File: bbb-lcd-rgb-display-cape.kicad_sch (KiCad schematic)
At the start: 28 parts, among them P12 RS485, P8 BeagleBone_Black_Header, P9 BeagleBone_Black_Header, Sw1 DTSM-31N, Sw2 DTSM-31N, Sw3 DTSM-31N, Sw4 DTSM-31N, U5 TCN75A, U6 DS18B20U

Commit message: Continue schematic work
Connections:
- net BACKLIGHT_PWM: now reaches P8.13 (Pin_13)
- net R1: now reaches P8.15 (Pin_15)
- net R0: now reaches P8.16 (Pin_16)
- net VSYNC: now reaches P8.27 (Pin_27)
- net PCLK: now reaches P8.28 (Pin_28)
- net HSYNC: now reaches P8.29 (Pin_29)
- net DE: now reaches P8.30 (Pin_30)
- net R3: now reaches P8.31 (Pin_31)
- net R2: now reaches P8.32 (Pin_32)
- net R4: now reaches P8.33 (Pin_33)
- net G0: now reaches P8.34 (Pin_34)
- net R5: now reaches P8.35 (Pin_35)
- net G1: now reaches P8.36 (Pin_36)
- net G3: now reaches P8.37 (Pin_37)
- net G2: now reaches P8.38 (Pin_38)
- net G5: now reaches P8.39 (Pin_39)
- net G4: now reaches P8.40 (Pin_40)
- net B1: now reaches P8.41 (Pin_41)
- net B0: now reaches P8.42 (Pin_42)
- net B3: now reaches P8.43 (Pin_43)
- net B2: now reaches P8.44 (Pin_44)
- net B5: now reaches P8.45 (Pin_45)
- net B4: now reaches P8.46 (Pin_46)
- no-connect marks 52 -> 29
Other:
- sheet LCD Display ports: added BACKLIGHT_PWM, LCD_CS, LCD_D0(B1), LCD_D1(B2), LCD_D10(G5), LCD_D11(R1), LCD_D12(R2), LCD_D13(R3), LCD_D14(R4), LCD_D15(R5), LCD_D2(B3), LCD_D3(B4), LCD_D4(B5), LCD_D5(G0), LCD_D6(G1), LCD_D7(G2), LCD_D8(G3), LCD_D9(G4), LCD_FMARK(PCLK), LCD_RD(VSYNC), LCD_RS(HSYNC), LCD_RST, LCD_SPI_CLK, LCD_SPI_CS0, LCD_SPI_DIO, LCD_WR(DE), POWER_SUPPLY_2.7-5.5V, POWER_SUPPLY_2.7-5.5V_GND, TP_I2C_SCL, TP_I2C_SDA, TP_IRQ, TP_SHUTDOWN; removed none
- moved on the sheet: P8

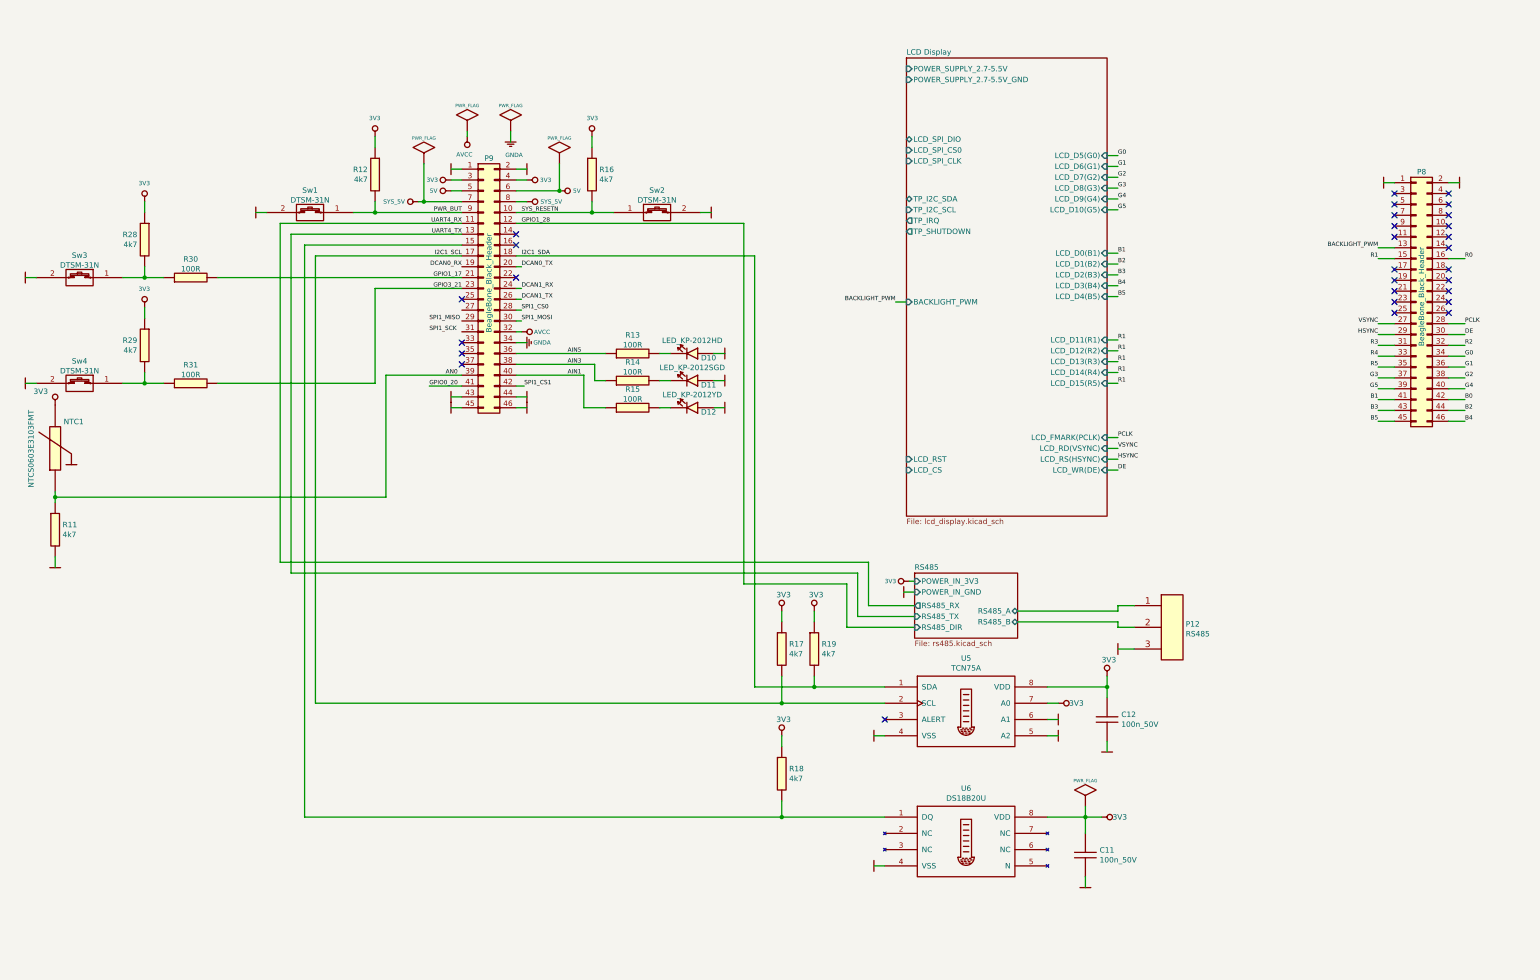
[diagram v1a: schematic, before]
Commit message: Corrected schematic and added new elements
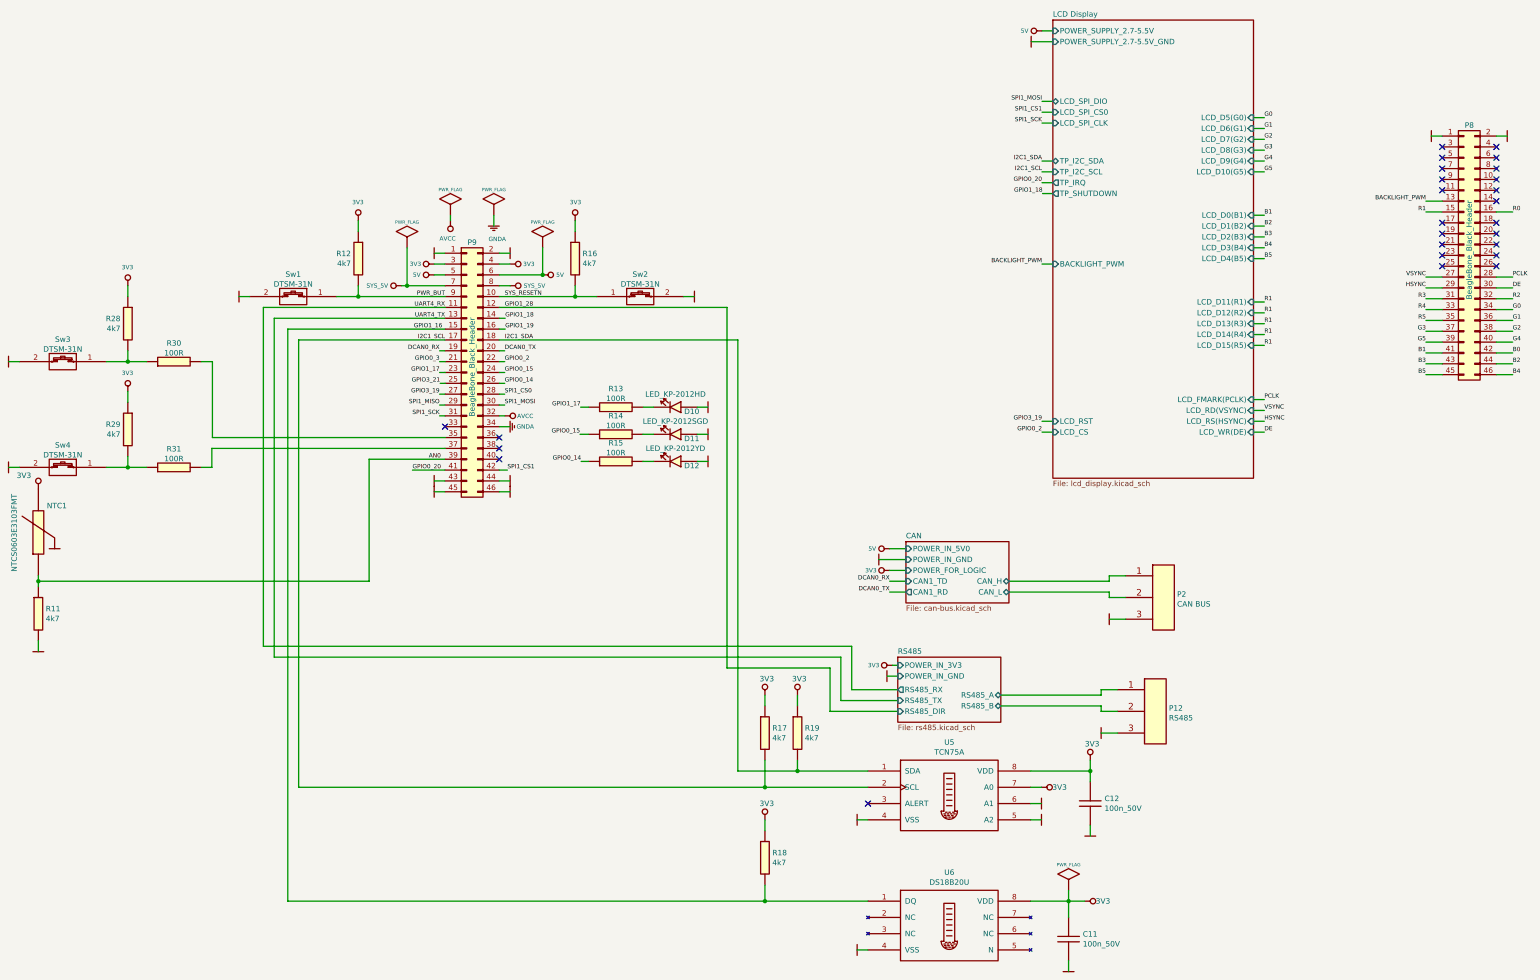
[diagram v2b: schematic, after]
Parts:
- added P2: CAN BUS, Discrete_Connectors:DG301-5.0-03P-12-00A(H), symbol Discrete_Connectors:DG301-5.0-03P-12-00A(H)
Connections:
- net GND: now also P2.3
- net GPIO1_17: now also P9.23 (Pin_23), R13.1; no longer P9.21 (Pin_21), R30.2
- net GPIO3_21: now also P9.25 (Pin_25); no longer P9.23 (Pin_23), R31.2
- net SPI1_MISO: now also P9.29 (Pin_29)
- net SPI1_SCK: now also P9.31 (Pin_31)
- net GPIO1_18: now reaches P9.14 (Pin_14)
- net GPIO1_16: now reaches P9.15 (Pin_15), R18.2, U6.1 (DQ)
- net GPIO1_19: now reaches P9.16 (Pin_16)
- net GPIO0_2: now reaches P9.22 (Pin_22)
- net GPIO3_19: now reaches P9.27 (Pin_27)
- net at P9.35 (Pin_35): now also R30.2
- net at P9.37 (Pin_37): now also R31.2
- net AIN1: no longer names the net of P9.40 (Pin_40)
- net AIN1: no longer R15.1
- net AIN3: no longer names the net of P9.38 (Pin_38)
- net AIN3: no longer R14.1
- net AIN5: no longer names the net of P9.36 (Pin_36)
- net AIN5: no longer R13.1
- net DCAN1_RX renamed GPIO0_15
- net GPIO0_15: now also R14.1
- net DCAN1_TX renamed GPIO0_14
- net GPIO0_14: now also R15.1
- new net CAN/CAN_H: P2.1
- new net CAN/CAN_L: P2.2
- new net GPIO0_3: P9.21 (Pin_21)
- no-connect marks 29 -> 26
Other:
- added sheet CAN (can-bus.kicad_sch)
- moved on the sheet: C11, C12, D10, D11, D12, NTC1, P12, P8, P9, R11, R12, R13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

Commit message: RC1
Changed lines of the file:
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@@
     (effects (font (size 1 1)) (justify left bottom))
   )
-  (label "R1" (at 331.47 96.52 0)
+  (label "R2" (at 331.47 96.52 0)
     (effects (font (size 1 1)) (justify left bottom))
   )
-  (label "R1" (at 331.47 99.06 0)
+  (label "R3" (at 331.47 99.06 0)
     (effects (font (size 1 1)) (justify left bottom))
   )
-  (label "R1" (at 331.47 101.6 0)
+  (label "R4" (at 331.47 101.6 0)
     (effects (font (size 1 1)) (justify left bottom))
   )
-  (label "R1" (at 331.47 104.14 0)
+  (label "R5" (at 331.47 104.14 0)
     (effects (font (size 1 1)) (justify left bottom))
   )
